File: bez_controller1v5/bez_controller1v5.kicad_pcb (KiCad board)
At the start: 4 copper layers, 100 x 60 mm, 79 parts, among them J1 Conn_01x03_Male, J10 Conn_01x07_Socket, J11 Conn_01x03_Male, J12 Conn_01x03_Male, J13 USB_B_Mini, J14 JTAG Conn_01x06_Male, J2 Conn_01x03_Male, J3 Conn_01x03_Male, J4 Screw_Terminal_01x02, J5 Conn_01x03_Male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

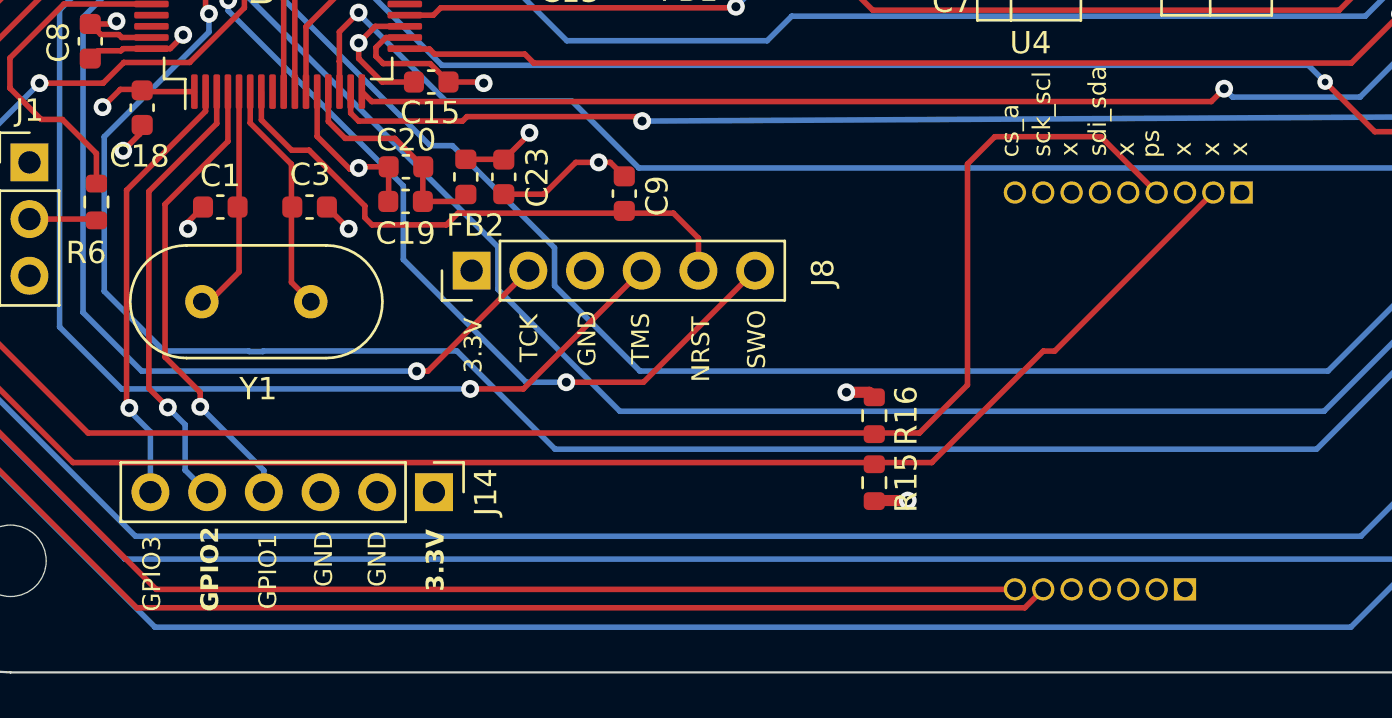
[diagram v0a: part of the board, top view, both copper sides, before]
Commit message: fix imu pin position, connect SDO pin to ground, change i2c resistors from 40k to 4k
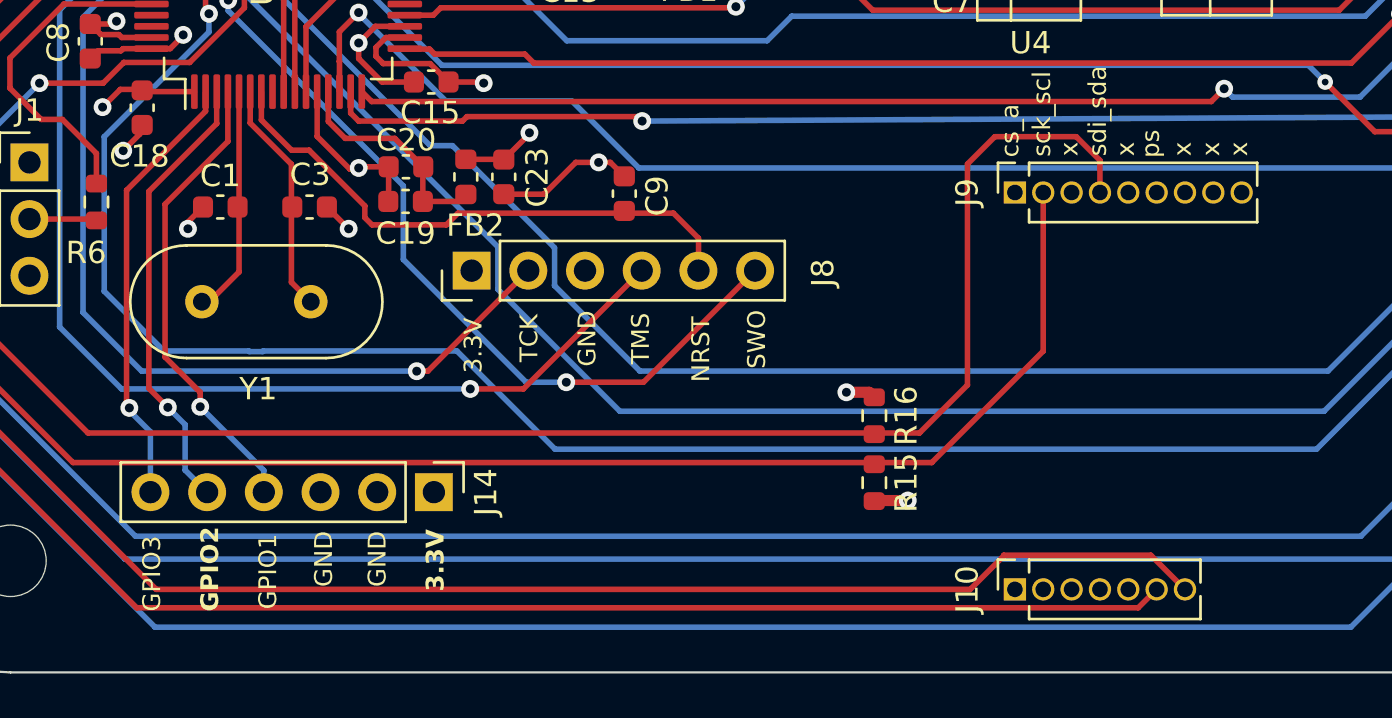
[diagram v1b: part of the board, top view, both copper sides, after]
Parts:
- J10, J9: moved to F.Cu
- moved J9 10.2 mm to (80.0, 64.5)
- moved J10 7.62 mm to (80.0, 82.3)
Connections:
- J9 pad 3: unconnected-(J9-Pin_3-Pad3) -> GND
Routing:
- net /INT2: track 79.6 -> 88.5 mm
- net /INT1: track 85.1 -> 90.2 mm
- net /SCK_SCL: track 87.1 -> 83.7 mm
- net /SDI_SDA: track 87.4 -> 85.7 mm

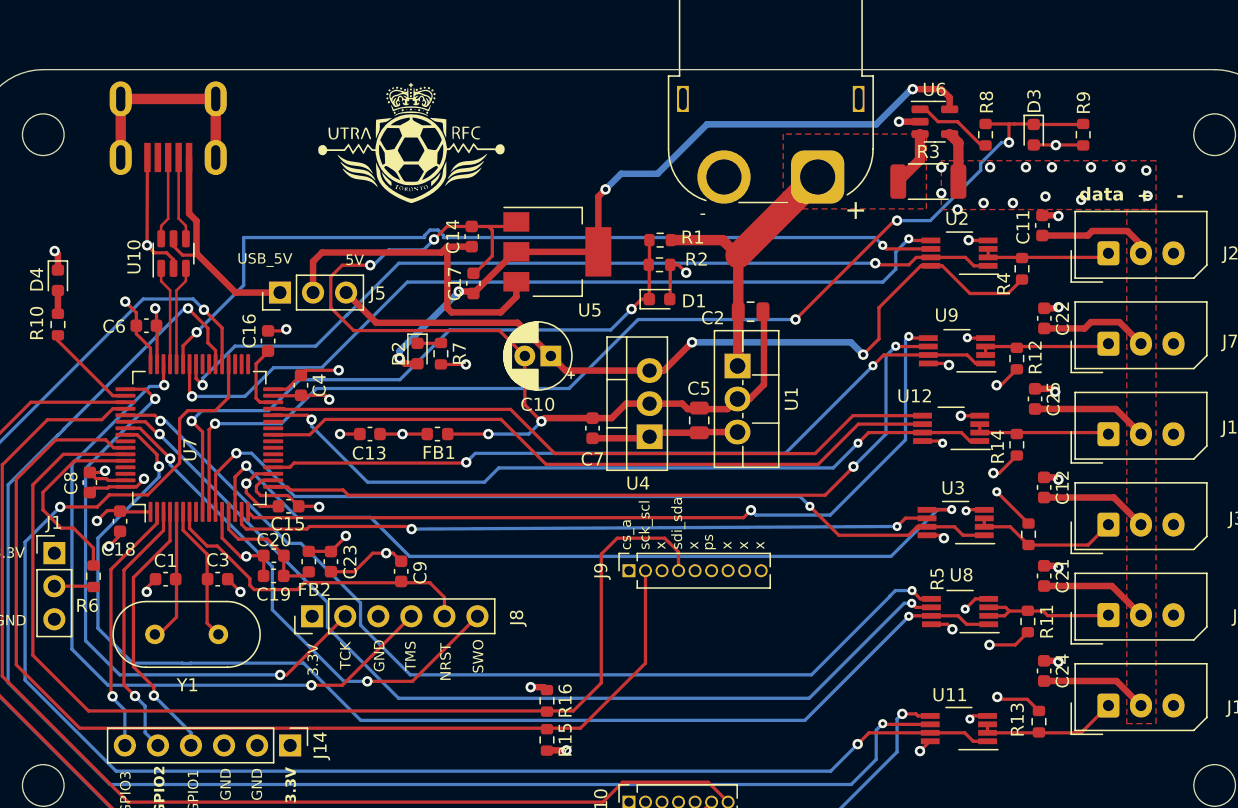
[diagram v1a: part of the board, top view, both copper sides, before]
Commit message: add old IMU
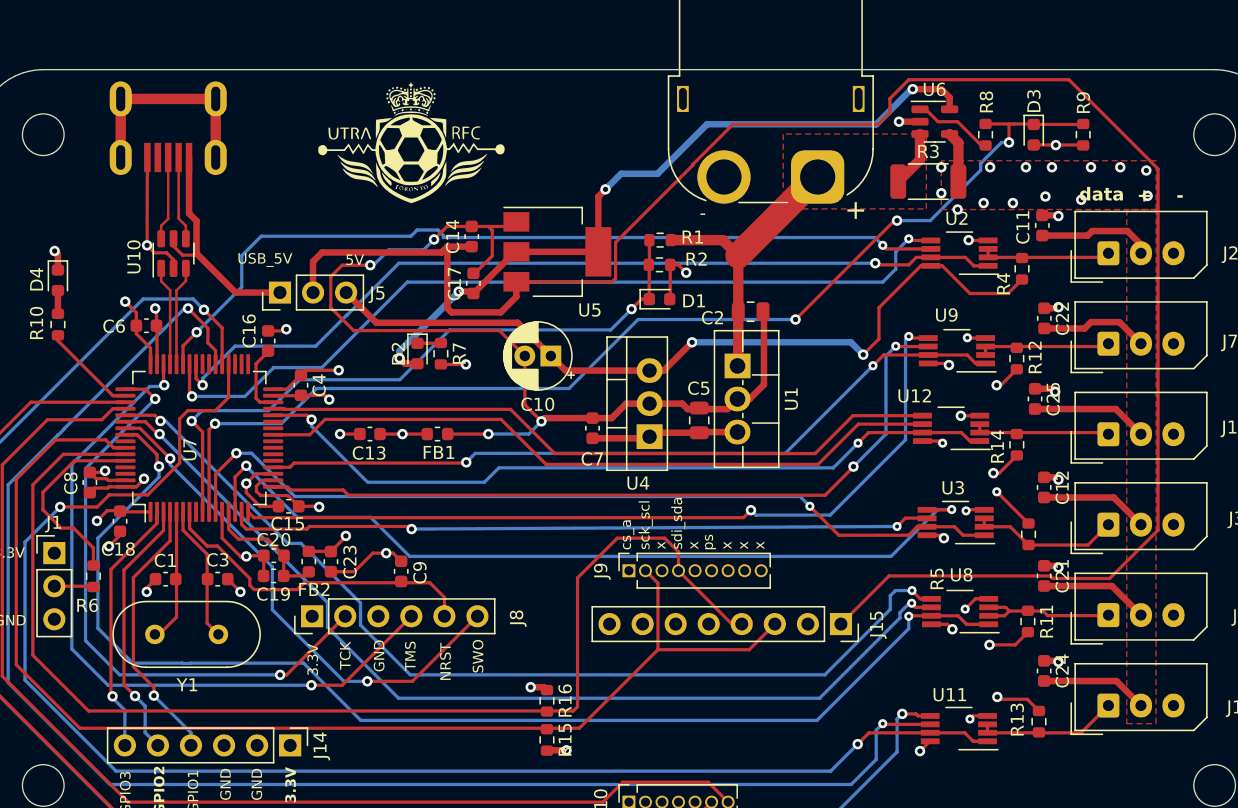
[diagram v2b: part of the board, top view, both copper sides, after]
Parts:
- added J15: IMU Conn_01x08_Female, Connector_PinSocket_2.54mm:PinSocket_1x08_P2.54mm_Vertical, F.Cu at (96.3, 68.6)
- R15, R16: value 40k -> 4k
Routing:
- net /power: track 26.9 -> 143.0 mm
- net /SCK_SCL: track 83.7 -> 94.2 mm
- net /SDI_SDA: track 85.7 -> 92.3 mm
- net /USART1_RX: track 65.5 -> 64.7 mm
- net /USART5_TX: track 74.1 -> 74.7 mm
- net /USART5_DIR: track 93.7 -> 94.3 mm

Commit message: fianl PCB review before ordering
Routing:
- net /power: track 143.0 -> 146.2 mm
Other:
- board text added: "Leonard Nam Chae Joanne"
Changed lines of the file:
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@@
       (drillshape 0)
       (scaleselection 1)
-      (outputdirectory "manufacturing/")
+      (outputdirectory "Manufacturing/")
     )
   )
@@
   (gr_line (start 35 26) (end 125 26)
     (stroke (width 0.1) (type default)) (layer "Edge.Cuts"))
+  (gr_text "Leonard\nNam\nChae\nJoanne" (at 118.55 84.8) (layer "B.Cu")
+    (effects (font (size 1 1.5) (thickness 0.25) bold) (justify left bottom mirror))
+  )
   (gr_text "GPIO2" (at 44.4 83.275 90) (layer "F.SilkS")
     (effects (font (size 0.8 0.8) (thickness 0.15) bold) (justify left bottom))
@@
     (effects (font (size 0.8 0.8) (thickness 0.15)) (justify left bottom))
   )
+  (gr_text "Leonard\nNam\nChae\nJoanne" (at 110.05 84.8) (layer "F.SilkS")
+    (effects (font (size 1 1) (thickness 0.15)) (justify left bottom))
+  )
   (gr_text "x" (at 87.975 62.875 90) (layer "F.SilkS")
     (effects (font (size 0.8 0.8) (thickness 0.15)) (justify left bottom))
@@
   (segment (start 84.85 46.95) (end 97.05 46.95) (width 0.5) (layer "B.Cu") (net 5))
   (segment (start 97.05 46.95) (end 98 47.9) (width 0.5) (layer "B.Cu") (net 5))
-  (segment (start 116.936261 65.1) (end 120.65 61.386261) (width 0.25) (layer "F.Cu") (net 6))
   (segment (start 70.15 44.65) (end 71.35 43.45) (width 0.5) (layer "F.Cu") (net 6))
-  (segment (start 101.499695 26.775) (end 100.05 28.224695) (width 0.25) (layer "F.Cu") (net 6))
-  (segment (start 84.925 33.267931) (end 84.925 33.325) (width 0.25) (layer "F.Cu") (net 6))
-  (segment (start 120.65 61.386261) (end 120.65 33.624695) (width 0.25) (layer "F.Cu") (net 6))
+  (segment (start 100.05 28.224695) (end 100.05 29.3) (width 0.25) (layer "F.Cu") (net 6))
+  (segment (start 80.45 41.5) (end 78.65 43.3) (width 0.25) (layer "F.Cu") (net 6))
   (segment (start 65.5984 40.05) (end 66.0492 39.5992) (width 0.5) (layer "F.Cu") (net 6))
-  (segment (start 99.15 30.2) (end 87.992931 30.2) (width 0.25) (layer "F.Cu") (net 6))
   (segment (start 71.35 43.45) (end 71.35 42.3) (width 0.5) (layer "F.Cu") (net 6))
+  (segment (start 112.577818 65.1) (end 116.936261 65.1) (width 0.25) (layer "F.Cu") (net 6))
   (segment (start 66.0492 39.5992) (end 67.9196 39.5992) (width 0.5) (layer "F.Cu") (net 6))
+  (segment (start 112.377818 64.9) (end 112.577818 65.1) (width 0.25) (layer "F.Cu") (net 6))
   (segment (start 66.0492 44.3242) (end 66.375 44.65) (width 0.5) (layer "F.Cu") (net 6))
   (segment (start 66.0492 39.5992) (end 66.0492 44.3242) (width 0.5) (layer "F.Cu") (net 6))
-  (segment (start 112.577818 65.1) (end 116.936261 65.1) (width 0.25) (layer "F.Cu") (net 6))
   (segment (start 66.375 44.65) (end 70.15 44.65) (width 0.5) (layer "F.Cu") (net 6))
-  (segment (start 87.992931 30.2) (end 84.925 33.267931) (width 0.25) (layer "F.Cu") (net 6))
   (segment (start 56.425 40.05) (end 65.5984 40.05) (width 0.5) (layer "F.Cu") (net 6))
-  (segment (start 78.70962 42.3) (end 71.35 42.3) (width 0.25) (layer "F.Cu") (net 6))
-  (segment (start 99.99 64.9) (end 112.377818 64.9) (width 0.25) (layer "F.Cu") (net 6))
-  (segment (start 78.975 39.275) (end 78.975 42.03462) (width 0.25) (layer "F.Cu") (net 6))
-  (segment (start 120.65 33.624695) (end 113.800305 26.775) (width 0.25) (layer "F.Cu") (net 6))
+  (segment (start 99.15 30.2) (end 84.85 30.2) (width 0.25) (layer "F.Cu") (net 6))
+  (segment (start 120.65 61.386261) (end 120.65 33.624695) (width 0.25) (layer "F.Cu") (net 6))
+  (segment (start 78.65 43.3) (end 72.35 43.3) (width 0.25) (layer "F.Cu") (net 6))
+  (segment (start 84.85 30.2) (end 80.45 34.6) (width 0.25) (layer "F.Cu") (net 6))
+  (segment (start 113.800305 26.775) (end 101.499695 26.775) (width 0.25) (layer "F.Cu") (net 6))
   (segment (start 96.29 68.6) (end 99.99 64.9) (width 0.25) (layer "F.Cu") (net 6))
-  (segment (start 112.377818 64.9) (end 112.577818 65.1) (width 0.25) (layer "F.Cu") (net 6))
-  (segment (start 84.925 33.325) (end 78.975 39.275) (width 0.25) (layer "F.Cu") (net 6))
+  (segment (start 116.936261 65.1) (end 120.65 61.386261) (width 0.25) (layer "F.Cu") (net 6))
+  (segment (start 80.45 34.6) (end 80.45 41.5) (width 0.25) (layer "F.Cu") (net 6))
   (segment (start 55.7276 40.7474) (end 56.425 40.05) (width 0.5) (layer "F.Cu") (net 6))
   (segment (start 55.7276 43.1292) (end 55.7276 40.7474) (width 0.5) (layer "F.Cu") (net 6))
+  (segment (start 72.35 43.3) (end 71.35 42.3) (width 0.25) (layer "F.Cu") (net 6))
+  (segment (start 120.65 33.624695) (end 113.800305 26.775) (width 0.25) (layer "F.Cu") (net 6))
+  (segment (start 99.99 64.9) (end 112.377818 64.9) (width 0.25) (layer "F.Cu") (net 6))
+  (segment (start 101.499695 26.775) (end 100.05 28.224695) (width 0.25) (layer "F.Cu") (net 6))
   (segment (start 100.05 29.3) (end 99.15 30.2) (width 0.25) (layer "F.Cu") (net 6))
-  (segment (start 78.975 42.03462) (end 78.70962 42.3) (width 0.25) (layer "F.Cu") (net 6))
-  (segment (start 113.800305 26.775) (end 101.499695 26.775) (width 0.25) (layer "F.Cu") (net 6))
-  (segment (start 100.05 28.224695) (end 100.05 29.3) (width 0.25) (layer "F.Cu") (net 6))
   (segment (start 41.315 58.0552) (end 40.0448 58.0552) (width 0.25) (layer "F.Cu") (net 7))
   (segment (start 39.9198 59.8802) (end 40.7924 59.8802) (width 0.25) (layer "F.Cu") (net 7))
@@
   (segment (start 62.375 48.175) (end 62.375 47.625) (width 0.5) (layer "B.Cu") (net 7))
   (segment (start 62.375 47.625) (end 66.925 43.075) (width 0.5) (layer "B.Cu") (net 7))
-  (segment (start 101.7 27.5) (end 101.8 27.5) (width 0.5) (layer "B.Cu") (net 7))
-  (segment (start 78.2 35.2) (end 79.4 34) (width 0.5) (layer "B.Cu") (net 7))
-  (segment (start 82.2 34) (end 86 30.2) (width 0.5) (layer "B.Cu") (net 7))
+  (segment (start 79.4 34) (end 83.75 34) (width 0.5) (layer "B.Cu") (net 7))
   (segment (start 66.925 43.075) (end 66.925 43.05) (width 0.5) (layer "B.Cu") (net 7))
   (segment (start 99 30.2) (end 101.7 27.5) (width 0.5) (layer "B.Cu") (net 7))
-  (segment (start 79.4 34) (end 82.2 34) (width 0.5) (layer "B.Cu") (net 7))
-  (segment (start 86 30.2) (end 99 30.2) (width 0.5) (layer "B.Cu") (net 7))
+  (segment (start 83.75 34) (end 87.55 30.2) (width 0.5) (layer "B.Cu") (net 7))
+  (segment (start 101.7 27.5) (end 101.8 27.5) (width 0.5) (layer "B.Cu") (net 7))
+  (segment (start 87.55 30.2) (end 99 30.2) (width 0.5) (layer "B.Cu") (net 7))
+  (segment (start 78.2 35.2) (end 79.4 34) (width 0.5) (layer "B.Cu") (net 7))
   (segment (start 50 62.075) (end 52.2198 62.075) (width 0.25) (layer "F.Cu") (net 8))
   (segment (start 53.475 64.9) (end 53.475 63.365) (width 0.25) (layer "F.Cu") (net 8))
